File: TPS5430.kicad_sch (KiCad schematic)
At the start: 33 parts, among them J1 Barrel_Jack, J2 Screw_Terminal_01x02, Q1 AO3401A, U1 TPS5430DDA

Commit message: Add page description
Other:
- company: (none) -> Max Stabel
- title: (none) -> TPS5430
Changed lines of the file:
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@@
 (kicad_sch (version 20210621) (generator eeschema)
   (paper "A4")
+  (title_block
+    (title "TPS5430")
+    (date "2021-07-15")
+    (rev "1.0.0")
+    (company "Max Stabel")
+  )
   (junction (at 27.94 113.03) (diameter 0.9144) (color 0 0 0 0))
   (junction (at 39.37 113.03) (diameter 0.9144) (color 0 0 0 0))

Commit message: Add library with used extra parts
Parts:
- J1: footprint MyFootprints:DC-005-5A-2.0-SMT -> tps5430:DC-005-5A-2.0-SMT
- L1: footprint MyFootprints:L_Sunlord_MWSA1004S_10x11.5x4mm -> tps5430:L_Sunlord_MWSA1004S_10x11.5x4mm
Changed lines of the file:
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@@
     (property "Reference" "L1" (id 0) (at 114.3 111.76 90))
     (property "Value" "47u" (id 1) (at 114.3 114.3 90))
-    (property "Footprint" "MyFootprints:L_Sunlord_MWSA1004S_10x11.5x4mm" (id 2) (at 114.3 118.11 0)
+    (property "Footprint" "tps5430:L_Sunlord_MWSA1004S_10x11.5x4mm" (id 2) (at 114.3 118.11 0)
       (effects (font (size 1.27 1.27)) hide)
     )
@@
     (property "Reference" "J1" (id 0) (at 67.437 35.56 0))
     (property "Value" "Barrel_Jack" (id 1) (at 67.437 38.1 0))
-    (property "Footprint" "MyFootprints:DC-005-5A-2.0-SMT" (id 2) (at 67.31 45.466 0)
+    (property "Footprint" "tps5430:DC-005-5A-2.0-SMT" (id 2) (at 67.31 45.466 0)
       (effects (font (size 1.27 1.27)) hide)
     )
@@
     )
     (path "/997044a6-4b67-44cb-978a-cd0e5e620fbe"
-      (reference "J1") (unit 1) (value "Barrel_Jack") (footprint "MyFootprints:DC-005-5A-2.0-SMT")
+      (reference "J1") (unit 1) (value "Barrel_Jack") (footprint "tps5430:DC-005-5A-2.0-SMT")
     )
     (path "/1b77a39f-736d-495d-a603-89f2366d24c5"
@@
     )
     (path "/24782b93-d714-465d-be36-72a34ae0df9f"
-      (reference "L1") (unit 1) (value "47u") (footprint "MyFootprints:L_Sunlord_MWSA1004S_10x11.5x4mm")
+      (reference "L1") (unit 1) (value "47u") (footprint "tps5430:L_Sunlord_MWSA1004S_10x11.5x4mm")
     )
     (path "/9a318088-4d93-418f-afaf-4303a06e8293"

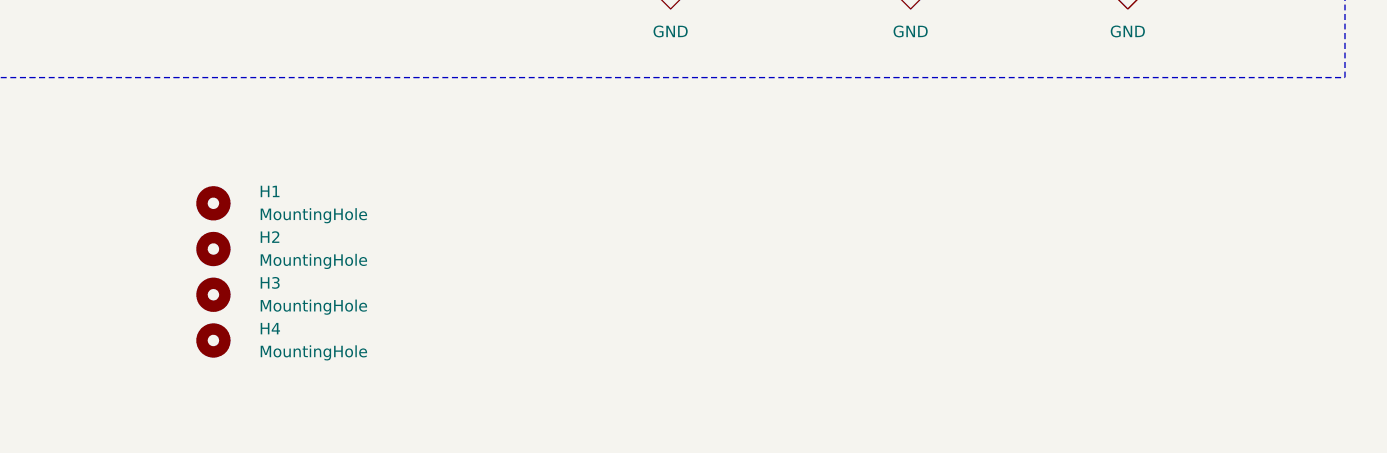
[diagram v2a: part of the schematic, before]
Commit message: Add License notice in files and on the PCB
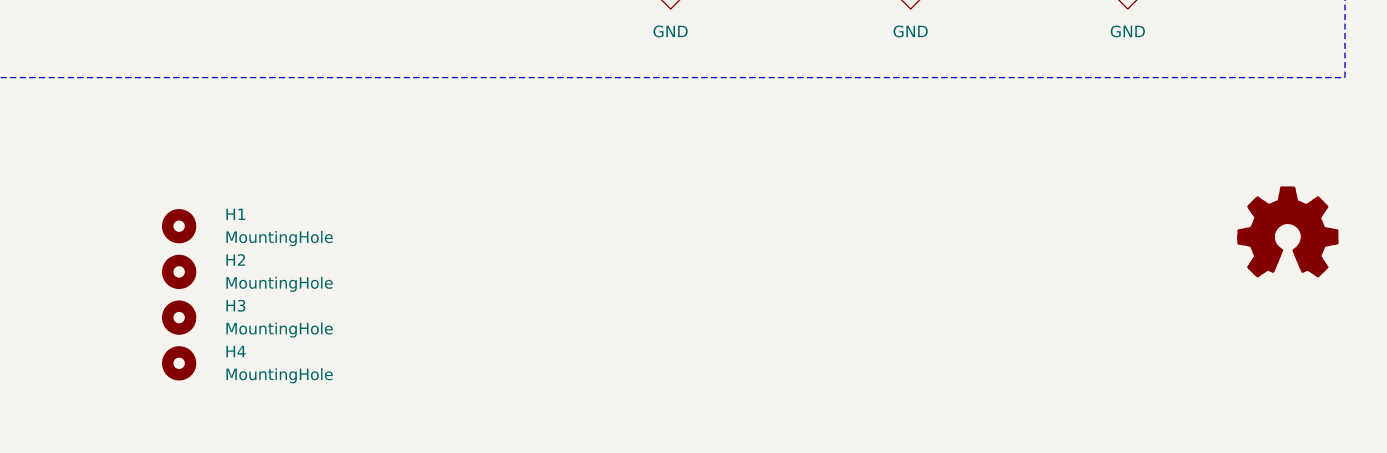
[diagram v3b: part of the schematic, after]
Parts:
- added LOGO1: Logo_Open_Hardware_Small, Symbol:OSHW-Logo_11.4x12mm_Copper, symbol Graphic:Logo_Open_Hardware_Small
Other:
- moved on the sheet: H1, H2, H3, H4
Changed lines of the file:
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@@
     (rev "1.0.0")
     (company "Max Stabel")
+    (comment 1 "https://github.com/M4a1x/TPS5430")
   )
   (junction (at 27.94 113.03) (diameter 0.9144) (color 0 0 0 0))
@@
     (pin "2")
   )
-  (symbol (lib_id "Mechanical:MountingHole") (at 157.48 170.18 270) (unit 1)
-    (in_bom yes) (on_board yes) (fields_autoplaced)
-    (property "Reference" "H1" (id 0) (at 162.56 168.9099 90)
-      (effects (font (size 1.27 1.27)) (justify left))
-    )
-    (property "Value" "MountingHole" (id 1) (at 162.56 171.4499 90)
-      (effects (font (size 1.27 1.27)) (justify left))
-    )
-    (property "Footprint" "MountingHole:MountingHole_2.2mm_M2_ISO7380" (id 2) (at 157.48 170.18 0)
-      (effects (font (size 1.27 1.27)) hide)
-    )
-    (property "Datasheet" "~" (id 3) (at 157.48 170.18 0)
-      (effects (font (size 1.27 1.27)) hide)
-    )
-  )
-  (symbol (lib_id "Mechanical:MountingHole") (at 157.48 175.26 270) (unit 1)
-    (in_bom yes) (on_board yes) (fields_autoplaced)
-    (property "Reference" "H2" (id 0) (at 162.56 173.9899 90)
-      (effects (font (size 1.27 1.27)) (justify left))
-    )
-    (property "Value" "MountingHole" (id 1) (at 162.56 176.5299 90)
-      (effects (font (size 1.27 1.27)) (justify left))
-    )
-    (property "Footprint" "MountingHole:MountingHole_2.2mm_M2_ISO7380" (id 2) (at 157.48 175.26 0)
-      (effects (font (size 1.27 1.27)) hide)
-    )
-    (property "Datasheet" "~" (id 3) (at 157.48 175.26 0)
-      (effects (font (size 1.27 1.27)) hide)
-    )
-  )
-  (symbol (lib_id "Mechanical:MountingHole") (at 157.48 180.34 270) (unit 1)
-    (in_bom yes) (on_board yes) (fields_autoplaced)
-    (property "Reference" "H3" (id 0) (at 162.56 179.0699 90)
-      (effects (font (size 1.27 1.27)) (justify left))
-    )
-    (property "Value" "MountingHole" (id 1) (at 162.56 181.6099 90)
-      (effects (font (size 1.27 1.27)) (justify left))
-    )
-    (property "Footprint" "MountingHole:MountingHole_2.2mm_M2_ISO7380" (id 2) (at 157.48 180.34 0)
-      (effects (font (size 1.27 1.27)) hide)
-    )
-    (property "Datasheet" "~" (id 3) (at 157.48 180.34 0)
-      (effects (font (size 1.27 1.27)) hide)
-    )
-  )
-  (symbol (lib_id "Mechanical:MountingHole") (at 157.48 185.42 270) (unit 1)
-    (in_bom yes) (on_board yes) (fields_autoplaced)
-    (property "Reference" "H4" (id 0) (at 162.56 184.1499 90)
-      (effects (font (size 1.27 1.27)) (justify left))
-    )
-    (property "Value" "MountingHole" (id 1) (at 162.56 186.6899 90)
-      (effects (font (size 1.27 1.27)) (justify left))
-    )
-    (property "Footprint" "MountingHole:MountingHole_2.2mm_M2_ISO7380" (id 2) (at 157.48 185.42 0)
-      (effects (font (size 1.27 1.27)) hide)
-    )
-    (property "Datasheet" "~" (id 3) (at 157.48 185.42 0)
+  (symbol (lib_id "Mechanical:MountingHole") (at 153.67 172.72 270) (unit 1)
+    (in_bom yes) (on_board yes) (fields_autoplaced)
+    (property "Reference" "H1" (id 0) (at 158.75 171.4499 90)
+      (effects (font (size 1.27 1.27)) (justify left))
+    )
+    (property "Value" "MountingHole" (id 1) (at 158.75 173.9899 90)
+      (effects (font (size 1.27 1.27)) (justify left))
+    )
+    (property "Footprint" "MountingHole:MountingHole_2.2mm_M2_ISO7380" (id 2) (at 153.67 172.72 0)
+      (effects (font (size 1.27 1.27)) hide)
+    )
+    (property "Datasheet" "~" (id 3) (at 153.67 172.72 0)
+      (effects (font (size 1.27 1.27)) hide)
+    )
+  )
+  (symbol (lib_id "Mechanical:MountingHole") (at 153.67 177.8 270) (unit 1)
+    (in_bom yes) (on_board yes) (fields_autoplaced)
+    (property "Reference" "H2" (id 0) (at 158.75 176.5299 90)
+      (effects (font (size 1.27 1.27)) (justify left))
+    )
+    (property "Value" "MountingHole" (id 1) (at 158.75 179.0699 90)
+      (effects (font (size 1.27 1.27)) (justify left))
+    )
+    (property "Footprint" "MountingHole:MountingHole_2.2mm_M2_ISO7380" (id 2) (at 153.67 177.8 0)
+      (effects (font (size 1.27 1.27)) hide)
+    )
+    (property "Datasheet" "~" (id 3) (at 153.67 177.8 0)
+      (effects (font (size 1.27 1.27)) hide)
+    )
+  )
+  (symbol (lib_id "Mechanical:MountingHole") (at 153.67 182.88 270) (unit 1)
+    (in_bom yes) (on_board yes) (fields_autoplaced)
+    (property "Reference" "H3" (id 0) (at 158.75 181.6099 90)
+      (effects (font (size 1.27 1.27)) (justify left))
+    )
+    (property "Value" "MountingHole" (id 1) (at 158.75 184.1499 90)
+      (effects (font (size 1.27 1.27)) (justify left))
+    )
+    (property "Footprint" "MountingHole:MountingHole_2.2mm_M2_ISO7380" (id 2) (at 153.67 182.88 0)
+      (effects (font (size 1.27 1.27)) hide)
+    )
+    (property "Datasheet" "~" (id 3) (at 153.67 182.88 0)
+      (effects (font (size 1.27 1.27)) hide)
+    )
+  )
+  (symbol (lib_id "Mechanical:MountingHole") (at 153.67 187.96 270) (unit 1)
+    (in_bom yes) (on_board yes) (fields_autoplaced)
+    (property "Reference" "H4" (id 0) (at 158.75 186.6899 90)
+      (effects (font (size 1.27 1.27)) (justify left))
+    )
+    (property "Value" "MountingHole" (id 1) (at 158.75 189.2299 90)
+      (effects (font (size 1.27 1.27)) (justify left))
+    )
+    (property "Footprint" "MountingHole:MountingHole_2.2mm_M2_ISO7380" (id 2) (at 153.67 187.96 0)
+      (effects (font (size 1.27 1.27)) hide)
+    )
+    (property "Datasheet" "~" (id 3) (at 153.67 187.96 0)
       (effects (font (size 1.27 1.27)) hide)
     )
@@
     (pin "2")
     (pin "3")
+  )
+  (symbol (lib_id "Graphic:Logo_Open_Hardware_Small") (at 276.86 173.99 0) (unit 1)
+    (in_bom yes) (on_board yes) (fields_autoplaced)
+    (property "Reference" "LOGO1" (id 0) (at 276.86 167.005 0)
+      (effects (font (size 1.27 1.27)) hide)
+    )
+    (property "Value" "Logo_Open_Hardware_Small" (id 1) (at 276.86 179.705 0)
+      (effects (font (size 1.27 1.27)) hide)
+    )
+    (property "Footprint" "Symbol:OSHW-Logo_11.4x12mm_Copper" (id 2) (at 276.86 173.99 0)
+      (effects (font (size 1.27 1.27)) hide)
+    )
+    (property "Datasheet" "~" (id 3) (at 276.86 173.99 0)
+      (effects (font (size 1.27 1.27)) hide)
+    )
   )
   (symbol (lib_id "Regulator_Switching:TPS5430DDA") (at 81.28 118.11 0) (unit 1)
@@
       (reference "L1") (unit 1) (value "47u") (footprint "tps5430:L_Sunlord_MWSA1004S_10x11.5x4mm")
     )
+    (path "/301643a6-6c8f-4ed6-b579-291e66485d9f"
+      (reference "LOGO1") (unit 1) (value "Logo_Open_Hardware_Small") (footprint "Symbol:OSHW-Logo_11.4x12mm_Copper")
+    )
     (path "/9a318088-4d93-418f-afaf-4303a06e8293"

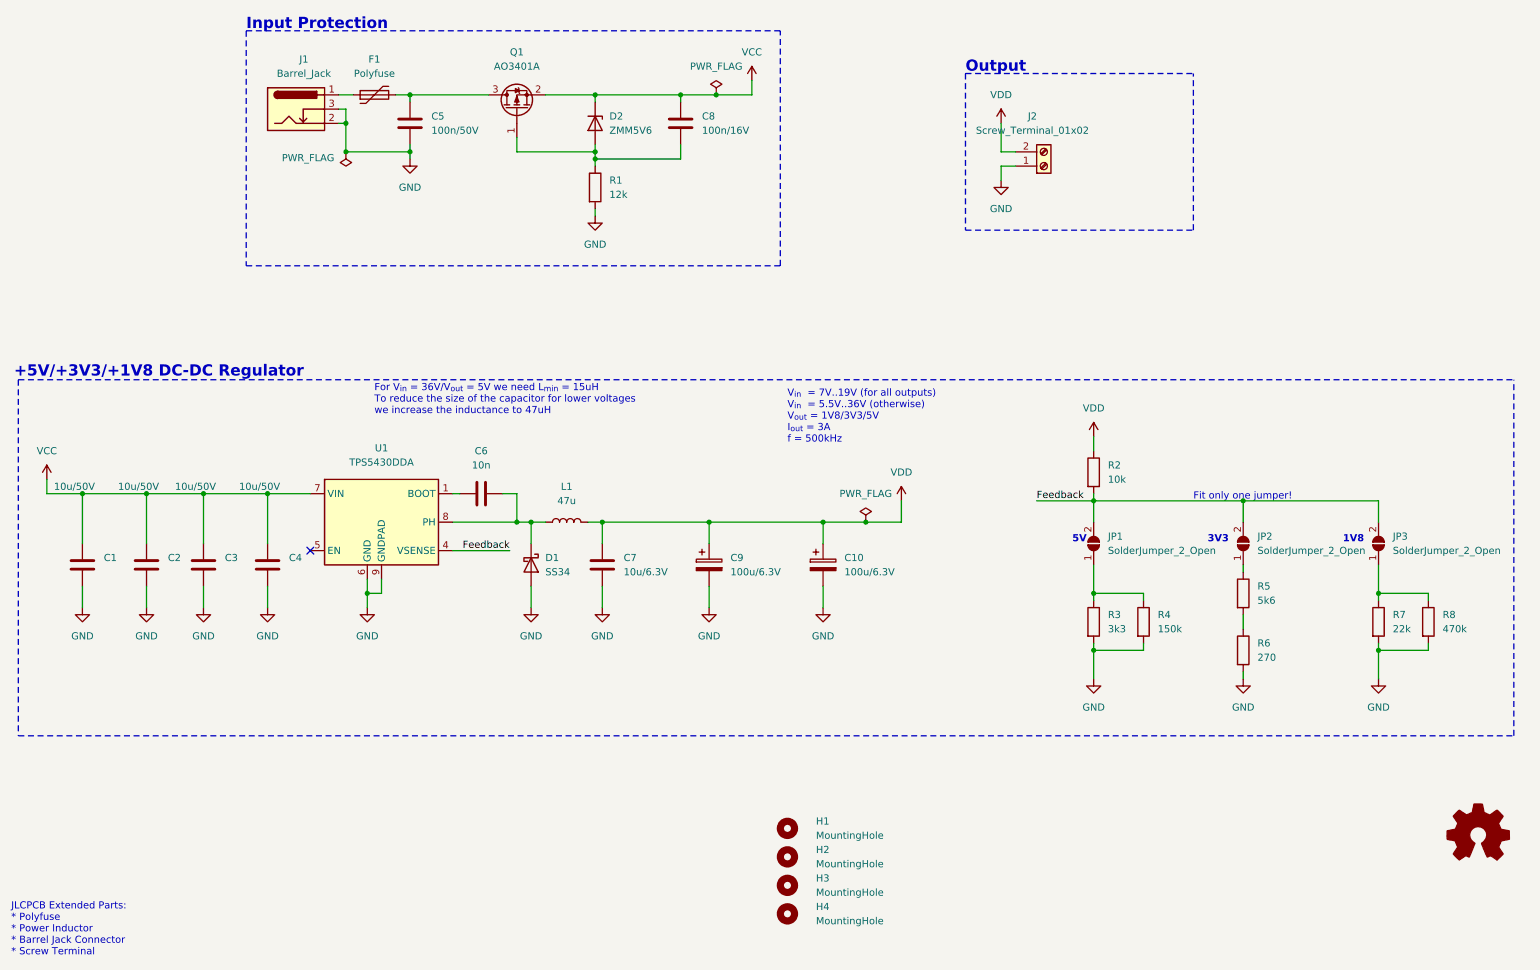
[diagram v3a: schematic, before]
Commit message: Add TP & 12V SolderJumper
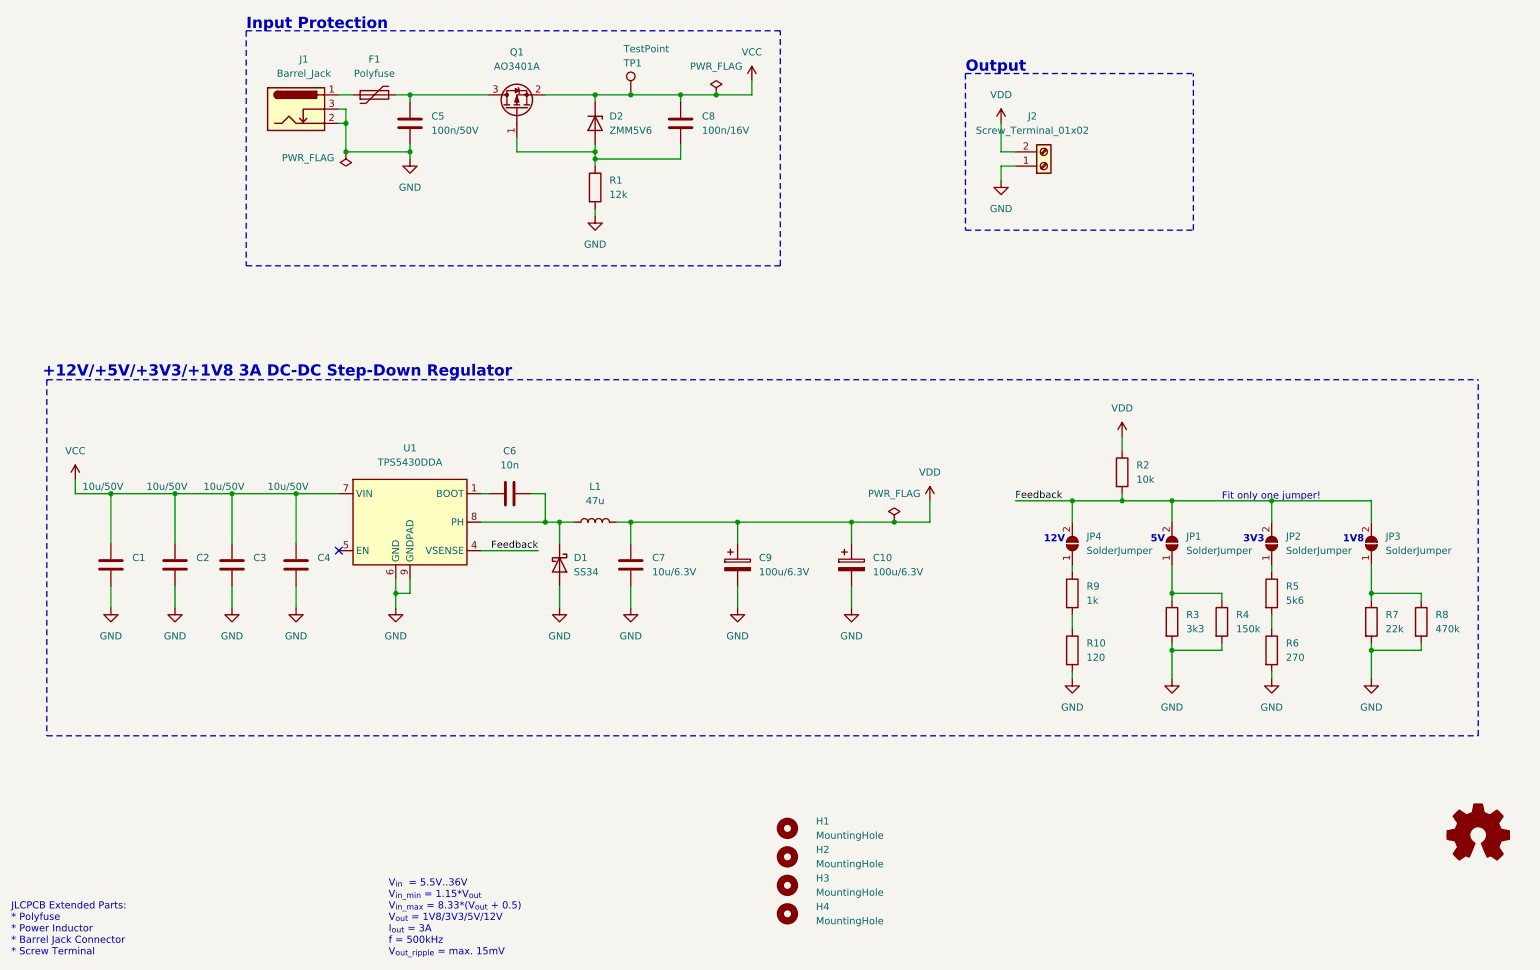
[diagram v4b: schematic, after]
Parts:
- added JP4: SolderJumper, Jumper:SolderJumper-2_P1.3mm_Open_RoundedPad1.0x1.5mm, symbol Jumper:SolderJumper_2_Open
- added R10: 120, Resistor_SMD:R_0402_1005Metric, symbol Device:R
- added R9: 1k, Resistor_SMD:R_0402_1005Metric, symbol Device:R
- added TP1: TestPoint, TestPoint:TestPoint_Pad_D1.0mm, symbol Connector:TestPoint
- JP1, JP2, JP3: value SolderJumper_2_Open -> SolderJumper
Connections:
- net Feedback: now also JP4.2 (B)
- net GND: now also R10.2
- net VCC: now also TP1.1
- new net: R10.1, R9.2
- new net: JP4.1 (A), R9.1
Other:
- note added: "+12V/+5V/+3V3/+1V8 3A DC-DC Step-Down Regulator"
- note added: "12V"
- note added: "V_{in} = 5.5V..36V V_{in_min} = 1.15*V_{out} V_{in_max} = 8.33*(V_{out} + 0.5) V_{out} = 1V8/3V3/5V/12V I_{out} = 3A f = 500kHz V_{out_ripple} = max. 15mV"
- note removed: "+5V/+3V3/+1V8 DC-DC Regulator"
- note removed: "For V_{in} = 36V/V_{out} = 5V we need L_{min} = 15uH To reduce the size of the capacitor for lower voltages we increase the inductance to 47uH"
- note removed: "V_{in} = 7V..19V (for all outputs) V_{in} = 5.5V..36V (otherwise) V_{out} = 1V8/3V3/5V I_{out} = 3A f = 500kHz"
- moved on the sheet: C1, C10, C2, C3, C4, C6, C7, C9, D1, JP1, JP2, JP3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
